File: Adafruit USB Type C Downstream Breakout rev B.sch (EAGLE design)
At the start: 8 parts

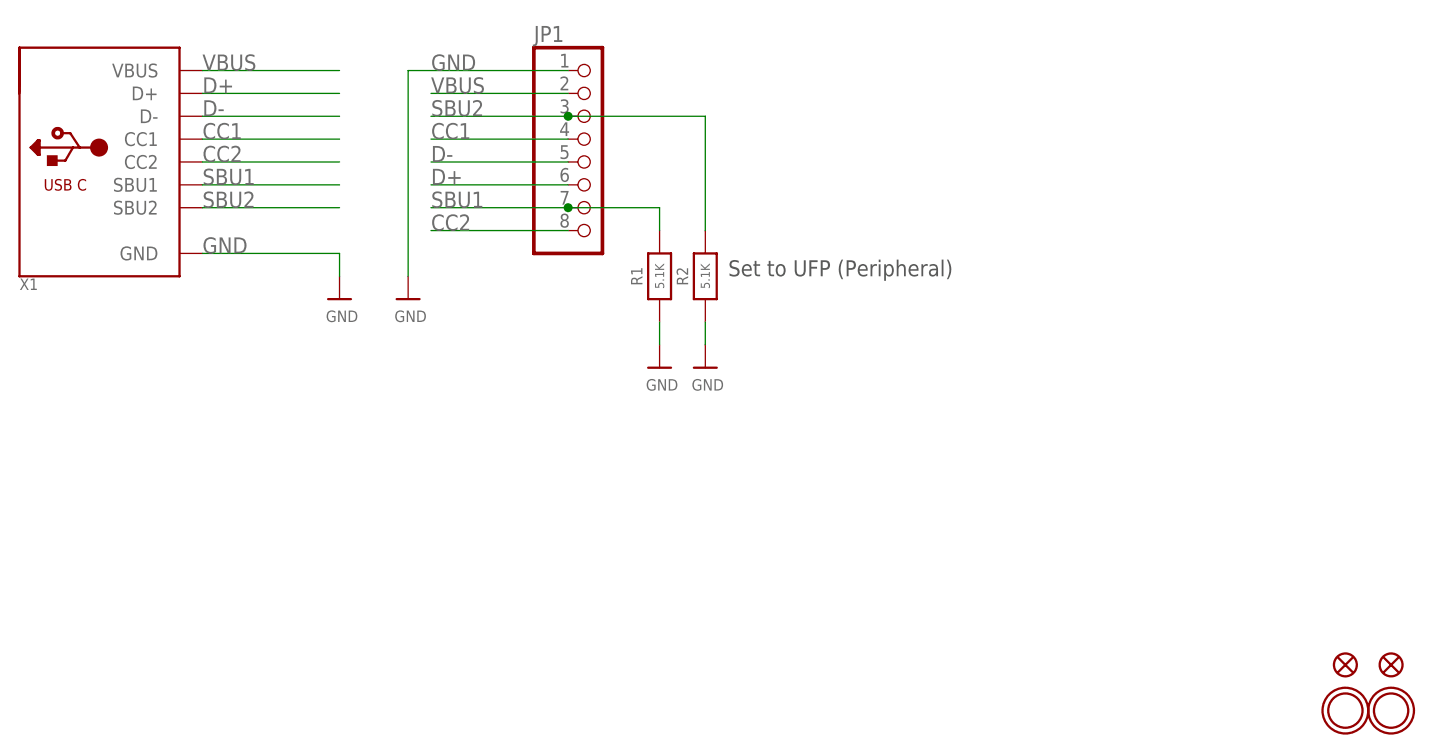
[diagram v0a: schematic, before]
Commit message: updating to rev b to fix issue #1
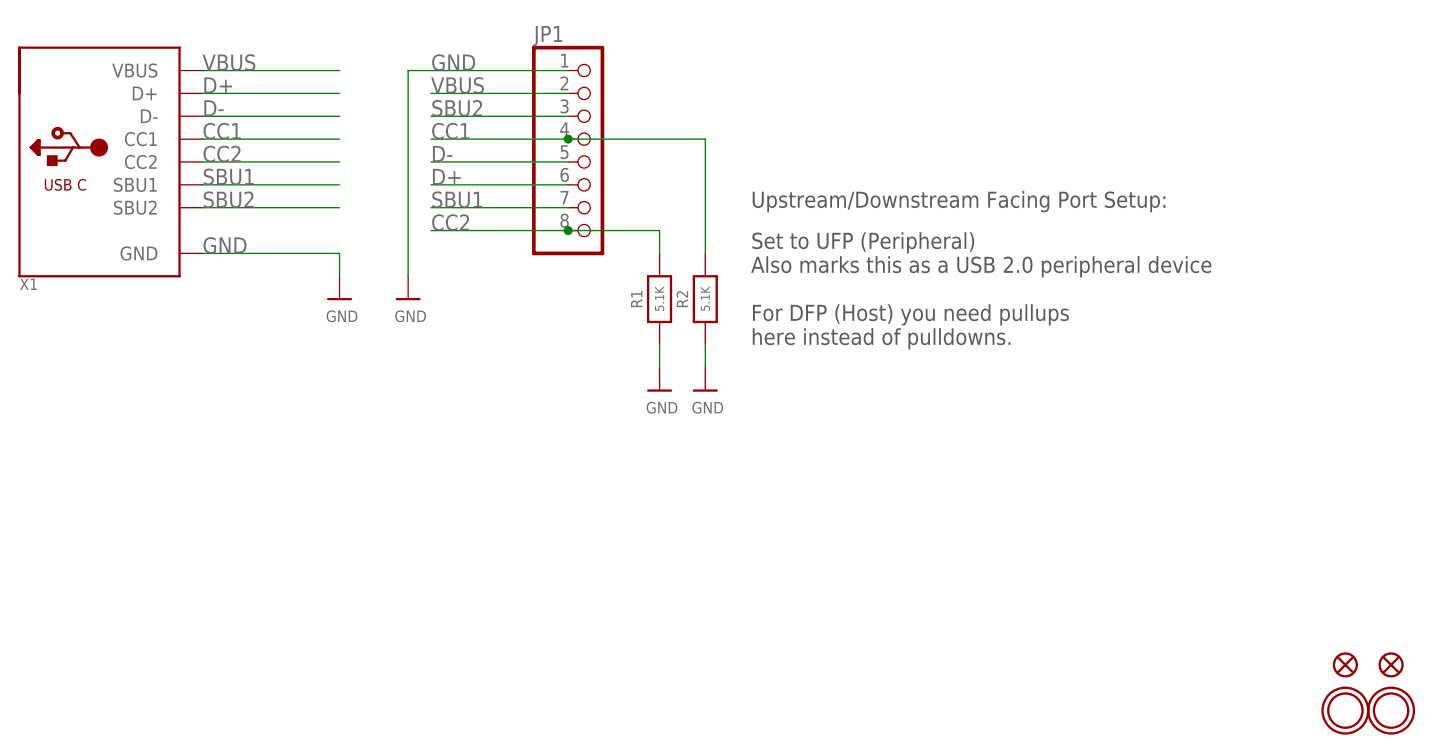
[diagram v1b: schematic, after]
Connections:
- net CC1: now also R2.2
- net CC2: now also R1.2
- net SBU1: no longer R1.2
- net SBU2: no longer R2.2
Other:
- note added: "Set to UFP (Peripheral) Also marks this as a USB 2.0 peripheral device For DFP (Host) you need pullups here instead of pulldowns."
- note added: "Upstream/Downstream Facing Port Setup:"
- note removed: "Set to UFP (Peripheral)"
- moved on the sheet: R1, R2
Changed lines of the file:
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@@
 <?xml version="1.0" encoding="utf-8"?>
 <!DOCTYPE eagle SYSTEM "eagle.dtd">
-<eagle version="9.2.0">
+<eagle version="9.3.0">
 <drawing>
 <settings>
-<setting alwaysvectorfont="no"/>
+<setting alwaysvectorfont="yes"/>
 <setting verticaltext="up"/>
 </settings>
@@
 <sheet>
 <plain>
-<text x="180.34" y="88.9" size="1.778" layer="97">Set to UFP (Peripheral)</text>
+<text x="182.88" y="81.28" size="1.778" layer="97">Set to UFP (Peripheral)
+Also marks this as a USB 2.0 peripheral device
+For DFP (Host) you need pullups
+here instead of pulldowns.</text>
+<text x="182.88" y="96.52" size="1.778" layer="97">Upstream/Downstream Facing Port Setup:</text>
 </plain>
 <instances>
-<instance part="FRAME1" gate="G$1" x="0" y="0"/>
-<instance part="FRAME1" gate="G$3" x="134.62" y="2.54">
+<instance part="FRAME1" gate="G$1" x="0" y="0" smashed="yes"/>
+<instance part="FRAME1" gate="G$3" x="134.62" y="2.54" smashed="yes">
 <attribute name="SHEET" x="243.5352" y="5.3848" size="2.54" layer="94" font="vector" ratio="10"/>
 <attribute name="DRAWING_NAME" x="167.6527" y="5.3848" size="2.54" layer="94" ratio="10"/>
@@
 <attribute name="REV" x="248.6152" y="21.2598" size="3.81" layer="94" ratio="12"/>
 </instance>
-<instance part="X1" gate="G$1" x="111.76" y="101.6">
+<instance part="X1" gate="G$1" x="111.76" y="101.6" smashed="yes">
 <attribute name="NAME" x="101.6" y="87.376" size="1.27" layer="95"/>
 <attribute name="VALUE" x="101.6" y="88.9" size="1.27" layer="96"/>
 </instance>
-<instance part="U$1" gate="G$1" x="254" y="40.64"/>
-<instance part="U$2" gate="G$1" x="248.92" y="40.64"/>
-<instance part="FID1" gate="G$1" x="254" y="45.72"/>
-<instance part="FID2" gate="G$1" x="248.92" y="45.72"/>
-<instance part="JP1" gate="A" x="165.1" y="101.6">
+<instance part="U$1" gate="G$1" x="254" y="40.64" smashed="yes"/>
+<instance part="U$2" gate="G$1" x="248.92" y="40.64" smashed="yes"/>
+<instance part="FID1" gate="G$1" x="254" y="45.72" smashed="yes"/>
+<instance part="FID2" gate="G$1" x="248.92" y="45.72" smashed="yes"/>
+<instance part="JP1" gate="A" x="165.1" y="101.6" smashed="yes">
 <attribute name="NAME" x="158.75" y="114.935" size="1.778" layer="95"/>
 <attribute name="VALUE" x="158.75" y="88.9" size="1.778" layer="96"/>
 </instance>
-<instance part="R1" gate="G$1" x="172.72" y="88.9" rot="R90">
-<attribute name="NAME" x="170.18" y="88.9" size="1.27" layer="95" font="vector" rot="R90" align="center"/>
-<attribute name="VALUE" x="172.72" y="88.9" size="1.016" layer="96" font="vector" ratio="15" rot="R90" align="center"/>
-</instance>
-<instance part="R2" gate="G$1" x="177.8" y="88.9" rot="R90">
-<attribute name="NAME" x="175.26" y="88.9" size="1.27" layer="95" font="vector" rot="R90" align="center"/>
-<attribute name="VALUE" x="177.8" y="88.9" size="1.016" layer="96" font="vector" ratio="15" rot="R90" align="center"/>
-</instance>
-<instance part="U$4" gate="G$1" x="172.72" y="78.74">
-<attribute name="VALUE" x="171.196" y="76.2" size="1.27" layer="96"/>
-</instance>
-<instance part="U$5" gate="G$1" x="177.8" y="78.74">
-<attribute name="VALUE" x="176.276" y="76.2" size="1.27" layer="96"/>
-</instance>
-<instance part="U$6" gate="G$1" x="137.16" y="86.36">
+<instance part="R1" gate="G$1" x="172.72" y="86.36" smashed="yes" rot="R90">
+<attribute name="NAME" x="170.18" y="86.36" size="1.27" layer="95" font="vector" rot="R90" align="center"/>
+<attribute name="VALUE" x="172.72" y="86.36" size="1.016" layer="96" font="vector" ratio="15" rot="R90" align="center"/>
+</instance>
+<instance part="R2" gate="G$1" x="177.8" y="86.36" smashed="yes" rot="R90">
+<attribute name="NAME" x="175.26" y="86.36" size="1.27" layer="95" font="vector" rot="R90" align="center"/>
+<attribute name="VALUE" x="177.8" y="86.36" size="1.016" layer="96" font="vector" ratio="15" rot="R90" align="center"/>
+</instance>
+<instance part="U$4" gate="G$1" x="172.72" y="76.2" smashed="yes">
+<attribute name="VALUE" x="171.196" y="73.66" size="1.27" layer="96"/>
+</instance>
+<instance part="U$5" gate="G$1" x="177.8" y="76.2" smashed="yes">
+<attribute name="VALUE" x="176.276" y="73.66" size="1.27" layer="96"/>
+</instance>
+<instance part="U$6" gate="G$1" x="137.16" y="86.36" smashed="yes">
 <attribute name="VALUE" x="135.636" y="83.82" size="1.27" layer="96"/>
 </instance>
-<instance part="U$7" gate="G$1" x="144.78" y="86.36">
+<instance part="U$7" gate="G$1" x="144.78" y="86.36" smashed="yes">
 <attribute name="VALUE" x="143.256" y="83.82" size="1.27" layer="96"/>
 </instance>
@@
 <pinref part="R1" gate="G$1" pin="1"/>
 <pinref part="U$4" gate="G$1" pin="GND"/>
-<wire x1="172.72" y1="83.82" x2="172.72" y2="81.28" width="0.1524" layer="91"/>
+<wire x1="172.72" y1="81.28" x2="172.72" y2="78.74" width="0.1524" layer="91"/>
 </segment>
 <segment>
 <pinref part="R2" gate="G$1" pin="1"/>
 <pinref part="U$5" gate="G$1" pin="GND"/>
-<wire x1="177.8" y1="83.82" x2="177.8" y2="81.28" width="0.1524" layer="91"/>
+<wire x1="177.8" y1="78.74" x2="177.8" y2="81.28" width="0.1524" layer="91"/>
 </segment>
 </net>
@@
 <pinref part="JP1" gate="A" pin="4"/>
 <label x="147.32" y="104.14" size="1.778" layer="95"/>
+<pinref part="R2" gate="G$1" pin="2"/>
+<wire x1="177.8" y1="104.14" x2="177.8" y2="91.44" width="0.1524" layer="91"/>
+<wire x1="162.56" y1="104.14" x2="177.8" y2="104.14" width="0.1524" layer="91"/>
+<junction x="162.56" y="104.14"/>
 </segment>
 </net>
@@
 <pinref part="JP1" gate="A" pin="8"/>
 <label x="147.32" y="93.98" size="1.778" layer="95"/>
+<pinref part="R1" gate="G$1" pin="2"/>
+<wire x1="172.72" y1="93.98" x2="172.72" y2="91.44" width="0.1524" layer="91"/>
+<wire x1="162.56" y1="93.98" x2="172.72" y2="93.98" width="0.1524" layer="91"/>
+<junction x="162.56" y="93.98"/>
 </segment>
 </net>
@@
 <pinref part="JP1" gate="A" pin="7"/>
 <label x="147.32" y="96.52" size="1.778" layer="95"/>
-<pinref part="R1" gate="G$1" pin="2"/>
-<wire x1="162.56" y1="96.52" x2="172.72" y2="96.52" width="0.1524" layer="91"/>
-<wire x1="172.72" y1="96.52" x2="172.72" y2="93.98" width="0.1524" layer="91"/>
-<junction x="162.56" y="96.52"/>
 </segment>
 </net>
@@
 <pinref part="JP1" gate="A" pin="3"/>
 <label x="147.32" y="106.68" size="1.778" layer="95"/>
-<pinref part="R2" gate="G$1" pin="2"/>
-<wire x1="162.56" y1="106.68" x2="177.8" y2="106.68" width="0.1524" layer="91"/>
-<wire x1="177.8" y1="106.68" x2="177.8" y2="93.98" width="0.1524" layer="91"/>
-<junction x="162.56" y="106.68"/>
 </segment>
 </net>
@@
 </schematic>
 </drawing>
+<compatibility>
+<note version="6.3" minversion="6.2.2" severity="warning">
+Since Version 6.2.2 text objects can contain more than one line,
+which will not be processed correctly with this version.
+</note>
+</compatibility>
 </eagle>
